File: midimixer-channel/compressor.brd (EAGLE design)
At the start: 185.4 x 49.5 mm, 99 parts, among them IC1 NE5532N, IC2 LM393N, IC3 LM3914N, IC4 TL072P, IC5 78L05Z, Q1 2N3906, Q2 2N3906, Q3 2N3906, T1 2N3904, T2 2N3904, T3 2N3904, U1 THAT4301P20-I

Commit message: wip
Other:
- board size 185.4 x 49.5 mm -> 177.8 x 49.5 mm
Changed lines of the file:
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@@
 <board>
 <plain>
-<wire x1="0" y1="-11.43" x2="185.4" y2="-11.43" width="0" layer="20"/>
-<wire x1="185.4" y1="-11.43" x2="185.4" y2="38.1" width="0" layer="20"/>
-<wire x1="185.4" y1="38.1" x2="0" y2="38.1" width="0" layer="20"/>
+<wire x1="0" y1="-11.43" x2="177.8" y2="-11.43" width="0" layer="20"/>
+<wire x1="177.8" y1="-11.43" x2="177.8" y2="38.1" width="0" layer="20"/>
+<wire x1="177.8" y1="38.1" x2="0" y2="38.1" width="0" layer="20"/>
 <wire x1="0" y1="38.1" x2="0" y2="-11.43" width="0" layer="20"/>
 </plain>

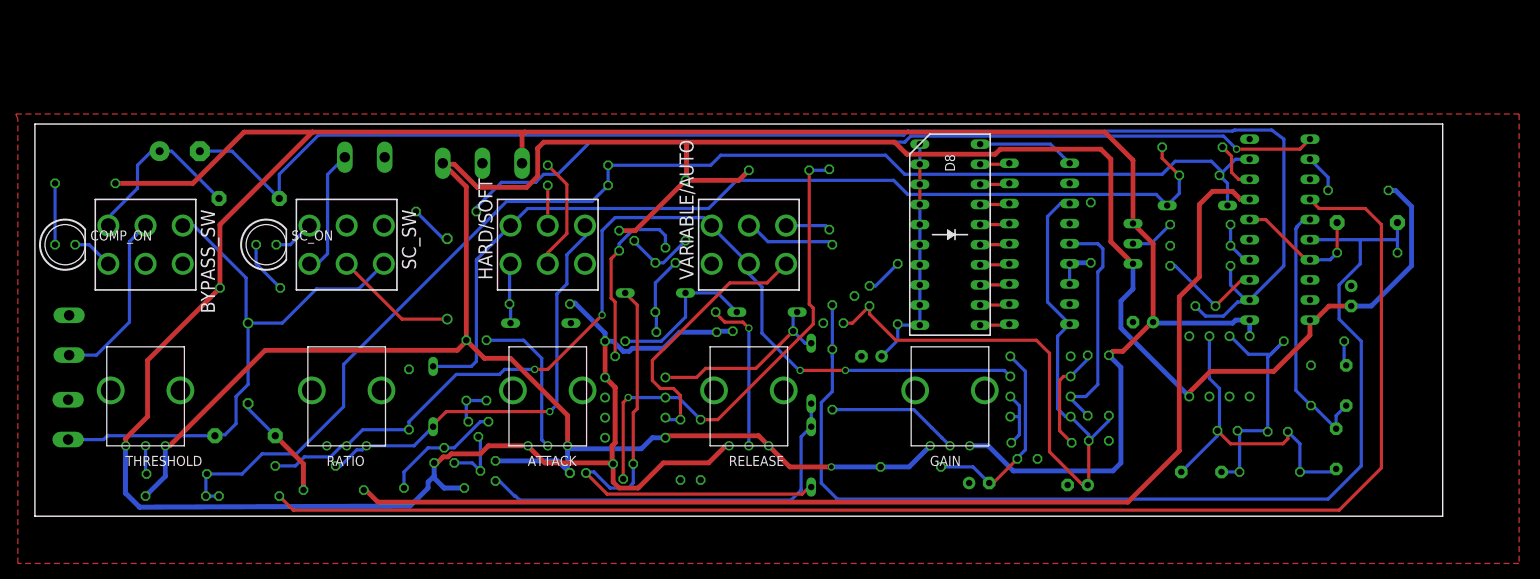
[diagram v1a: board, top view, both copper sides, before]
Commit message: compressor cleanups
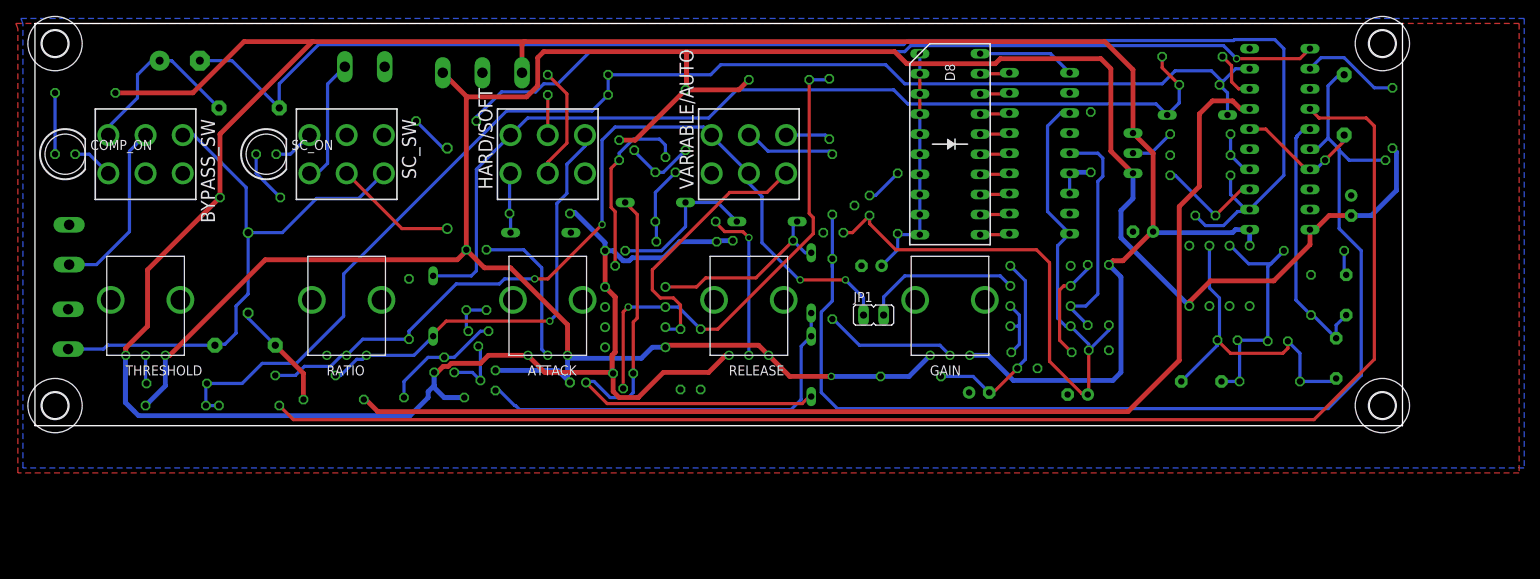
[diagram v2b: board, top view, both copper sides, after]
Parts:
- added H1, H2, H3, H4: MOUNT-HOLE3.3, holes:3,3
- added JP1: (no value), jumper:JP1
- moved C5 15.1 mm to (165.4, 40.5), turned to 90 degrees
- moved R6 11.8 mm to (166.8, 33.5)
- moved D1 11.4 mm to (146.8, 39.2)
- moved D8 11.4 mm to (115.6, 35.6)
- moved IC3 11.4 mm to (126.9, 34.4)
- moved Q3 11.4 mm to (73.8, 34.8)
- moved R20 11.4 mm to (100.3, 40.0)
- moved R4 11.4 mm to (140.0, 34.4)
- moved R9 11.4 mm to (51.9, 38.5)
- moved C15 11.4 mm to (161.2, 16.5)
- moved C20 11.4 mm to (105.7, 20.2)
- moved C7 11.4 mm to (165.6, 16.5)
- moved R34 11.4 mm to (135.6, 16.5)
- moved R35 11.4 mm to (133.0, 16.5)
- moved ATTACK 11.4 mm to (64.8, 8.89)
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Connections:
- new net N$67: IC4.3, JP1.2
- net GR_METER: now also JP1.1; no longer IC4.3
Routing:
- net N$67: track 0.00 -> 19.9 mm
- net GR_METER: track 125.2 -> 109.5 mm
- net -15V: track 358.0 -> 345.2 mm
- net N$15: track 4.88 -> 12.6 mm
- net N$9: track 140.7 -> 145.0 mm
- net N$12: track 183.2 -> 180.7 mm
- net N$8: track 17.3 -> 16.3 mm
- added copper zone on layer 16, net GND
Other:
- board size 177.8 x 49.5 mm -> 172.7 x 50.8 mm

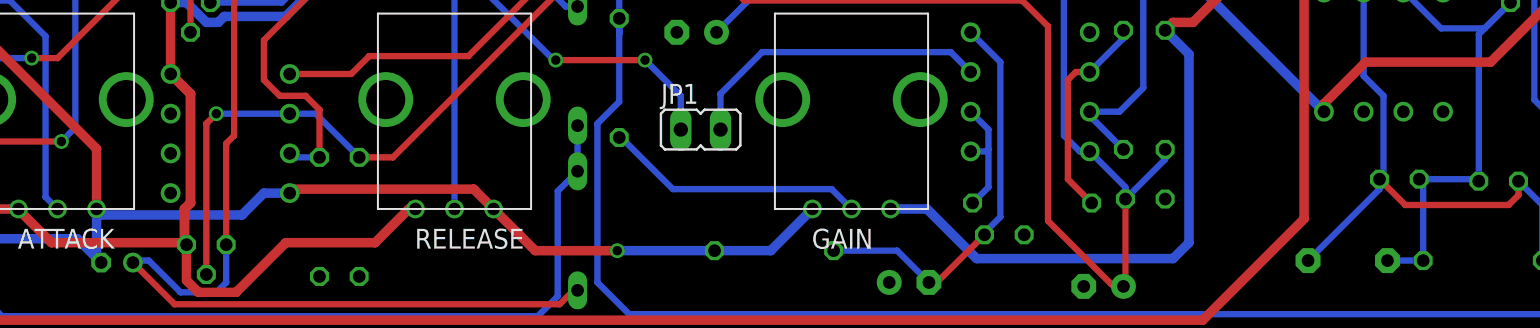
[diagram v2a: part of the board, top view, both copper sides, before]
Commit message: compressor: terminate opamps
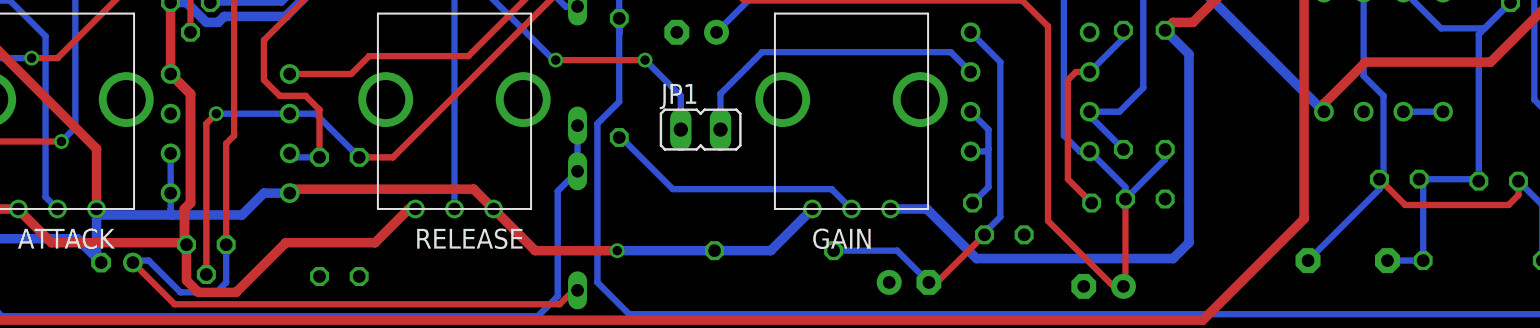
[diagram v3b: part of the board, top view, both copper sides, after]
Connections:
- new net N$68: IC1.1, IC1.2
- net -15V: now also IC2.5, IC2.6
- net GND: now also IC1.3
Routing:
- net -15V: track 345.2 -> 349.2 mm
- net N$68: track 0.00 -> 2.54 mm
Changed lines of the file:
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@@
 <vertex x="-1.524" y="50.8"/>
 </polygon>
+<contactref element="IC1" pad="3"/>
 </signal>
 <signal name="N$2">
@@
 <wire x1="79.629" y1="9.906" x2="77.978" y2="9.906" width="0.6096" layer="16"/>
 <wire x1="77.978" y1="9.906" x2="76.581" y2="8.509" width="0.6096" layer="16"/>
-<wire x1="76.581" y1="8.509" x2="67.397" y2="8.509" width="0.6096" layer="16"/>
+<wire x1="76.581" y1="8.509" x2="72.136" y2="8.509" width="0.6096" layer="16"/>
+<wire x1="72.136" y1="8.509" x2="67.397" y2="8.509" width="0.6096" layer="16"/>
 <wire x1="67.397" y1="8.509" x2="67.27" y2="8.382" width="0.6096" layer="16"/>
 <wire x1="91.4" y1="10.16" x2="79.883" y2="10.16" width="0.6096" layer="1"/>
@@
 <wire x1="171.958" y1="29.718" x2="171.958" y2="34.544" width="0.6096" layer="16"/>
 <wire x1="171.958" y1="34.544" x2="171.45" y2="35.052" width="0.6096" layer="16"/>
+<contactref element="IC2" pad="6"/>
+<contactref element="IC2" pad="5"/>
+<wire x1="72.009" y1="12.446" x2="72.009" y2="9.906" width="0.4064" layer="16"/>
+<wire x1="72.009" y1="8.89" x2="72.009" y2="8.636" width="0.4064" layer="16"/>
+<wire x1="72.009" y1="8.636" x2="72.136" y2="8.509" width="0.4064" layer="16"/>
+<wire x1="72.009" y1="9.906" x2="72.009" y2="8.89" width="0.4064" layer="16"/>
 </signal>
 <signal name="+15V">
@@
 <wire x1="121.92" y1="18.923" x2="123.19" y2="17.653" width="0.4064" layer="16"/>
 </signal>
+<signal name="N$68">
+<contactref element="IC1" pad="2"/>
+<contactref element="IC1" pad="1"/>
+<wire x1="153.416" y1="15.113" x2="150.876" y2="15.113" width="0.4064" layer="16"/>
+</signal>
 </signals>
